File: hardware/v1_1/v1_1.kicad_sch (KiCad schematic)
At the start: 77 parts, among them J1 AUDIO IN, J2 MIDI OUT, J3 MIDI IN, J4 MIDI THRU, J5 OUTPUT R, J6 OUTPUT L - MONO, J7 EXP 2, J8 EXP 1, J9 Batt In, SW1 RotaryEncoder_Switch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

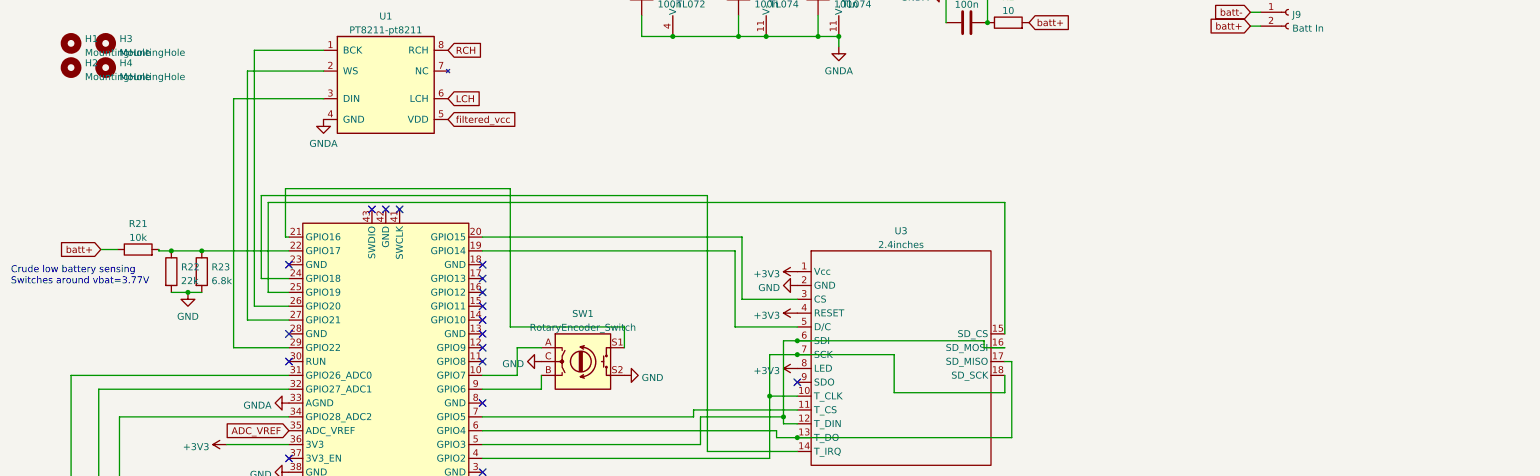
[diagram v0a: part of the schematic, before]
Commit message: Added ADC component
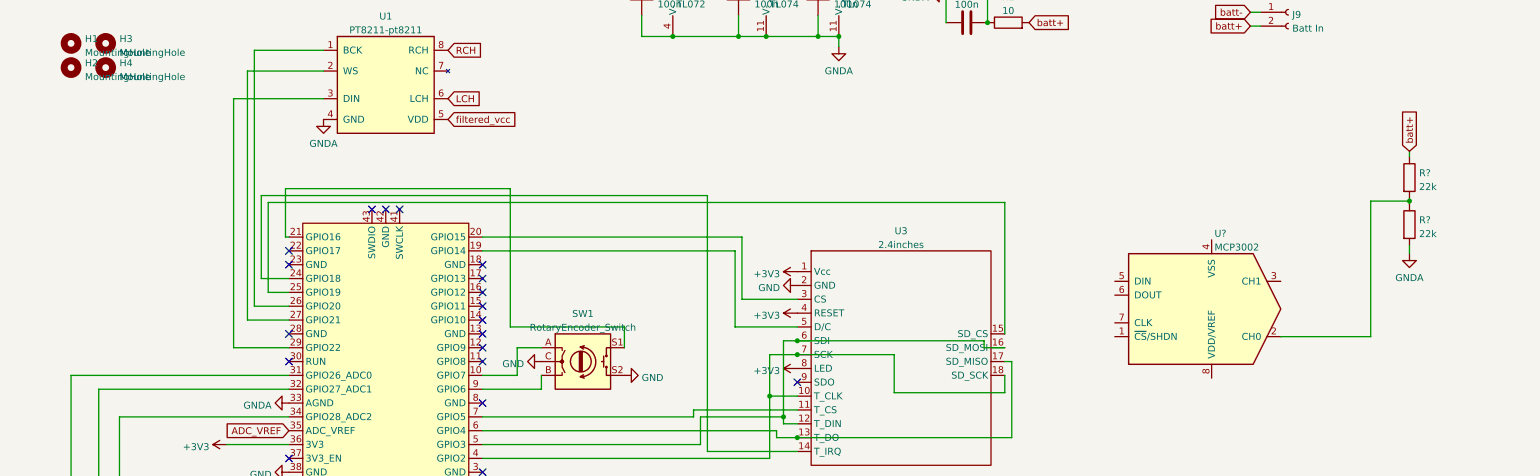
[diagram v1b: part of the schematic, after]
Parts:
- removed R21: 10k, Resistor_THT:R_Axial_DIN0207_L6.3mm_D2.5mm_P7.62mm_Horizontal, symbol Device:R
- removed R22: 22k, Resistor_THT:R_Axial_DIN0207_L6.3mm_D2.5mm_P7.62mm_Horizontal, symbol Device:R
- removed R23: 6.8k, Resistor_THT:R_Axial_DIN0207_L6.3mm_D2.5mm_P7.62mm_Horizontal, symbol Device:R
- added R? (x2): 22k, symbol Device:R
- added U?: MCP3002, symbol Analog_ADC:MCP3002
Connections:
- net GNDA: now also R?.2
- net batt+: now also R?.1
- new net: R?.1, R?.2, U?.2 (CH0)
- no-connect marks 45 -> 46
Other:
- note removed: "Crude low battery sensing Switches around vbat=3.77V"

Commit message: Added commnet
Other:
- note added: "Move TouchScreen to SPI1? Pin 10-13"
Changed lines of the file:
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@@
+    (effects (font (size 1.27 1.27)) (justify left bottom))
+  )
+  (text "Move TouchScreen to SPI1?\nPin 10-13" (at 155.448 112.014 0)
     (effects (font (size 1.27 1.27)) (justify left bottom))
   )

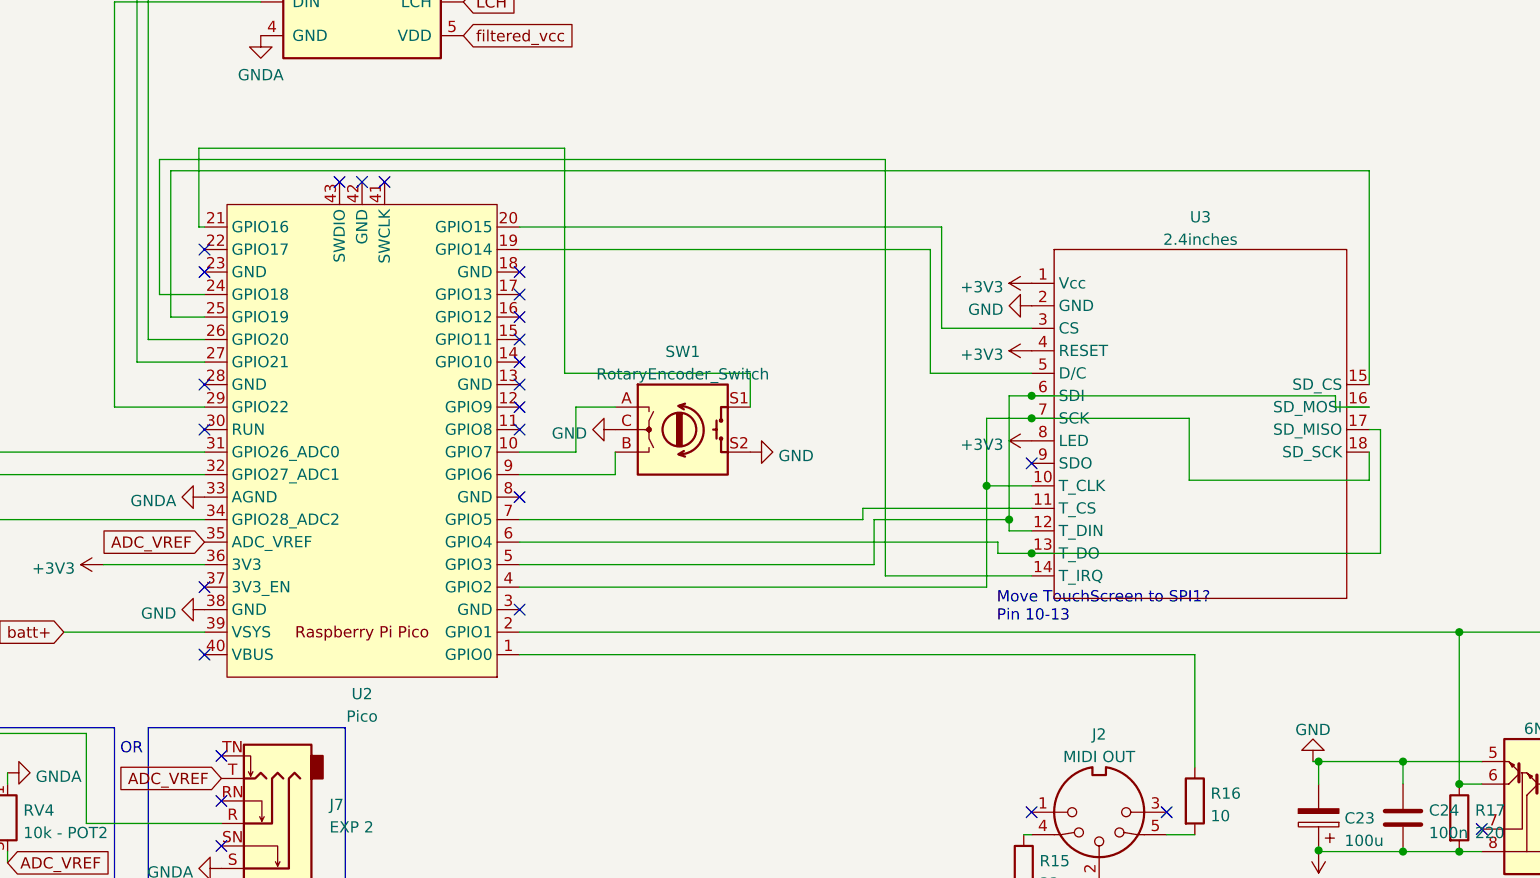
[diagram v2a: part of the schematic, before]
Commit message: Switch tacticle to SPI1
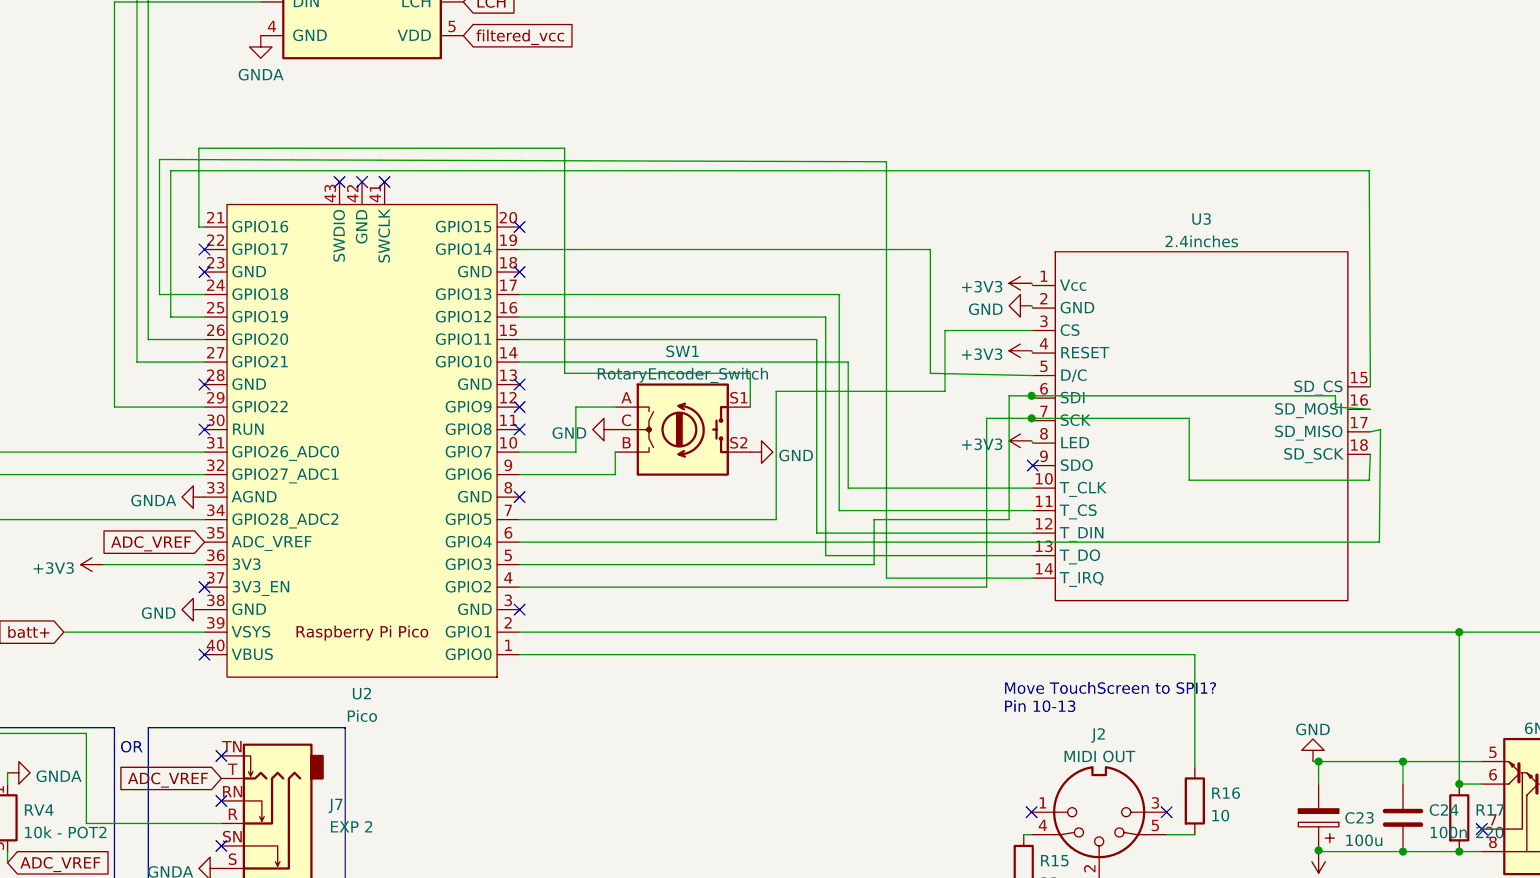
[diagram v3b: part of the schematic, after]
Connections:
- net at U2.14 (GPIO10): now also U3.10 (T_CLK)
- net at U2.15 (GPIO11): now also U3.12 (T_DIN)
- net at U2.16 (GPIO12): now also U3.13 (T_DO)
- net at U2.17 (GPIO13): now also U3.11 (T_CS)
- net at U2.20 (GPIO15): no longer U3.3 (CS)
- net at U2.4 (GPIO2), U3.18 (SD_SCK), U3.7 (SCK): no longer U3.10 (T_CLK)
- net at U2.5 (GPIO3), U3.16 (SD_MOSI), U3.6 (SDI): no longer U3.12 (T_DIN)
- net at U2.6 (GPIO4), U3.17 (SD_MISO): no longer U3.13 (T_DO)
- net at U2.7 (GPIO5): now also U3.3 (CS); no longer U3.11 (T_CS)
- no-connect marks 46 -> 43

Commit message: Added ADC for battery ctrl
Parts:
- added TP?: ADC IN1, symbol Connector:TestPoint
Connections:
- net ADC_VREF: now also U?.8 (VDD/VREF)
- net GNDA: now also U?.4 (VSS)
- net at U?.1 (~{CS}/SHDN): now also U2.12 (GPIO9)
- net at U?.3 (CH1): now also TP?.1
- net at U?.5 (DIN): now also U2.5 (GPIO3), U3.16 (SD_MOSI), U3.6 (SDI)
- net at U?.6 (DOUT): now also U2.6 (GPIO4), U3.17 (SD_MISO)
- net at U?.7 (CLK): now also U2.4 (GPIO2), U3.18 (SD_SCK), U3.7 (SCK)
- net at U2.20 (GPIO15): now also U3.3 (CS)
- net at U2.7 (GPIO5): no longer U3.3 (CS)
- no-connect marks 43 -> 42
